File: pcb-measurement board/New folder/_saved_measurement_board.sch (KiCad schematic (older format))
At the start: 92 parts, among them P1 HDR DUAL ROW, P2 CONN_02X15, P3 CONN_02X13, P4 CONN_02X05, P5 CONN_02X05, Q1 Si1101X, U1 NX3L4051, U10 TLV1G125, U11 NX3L4051, U12 MSP430G2955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

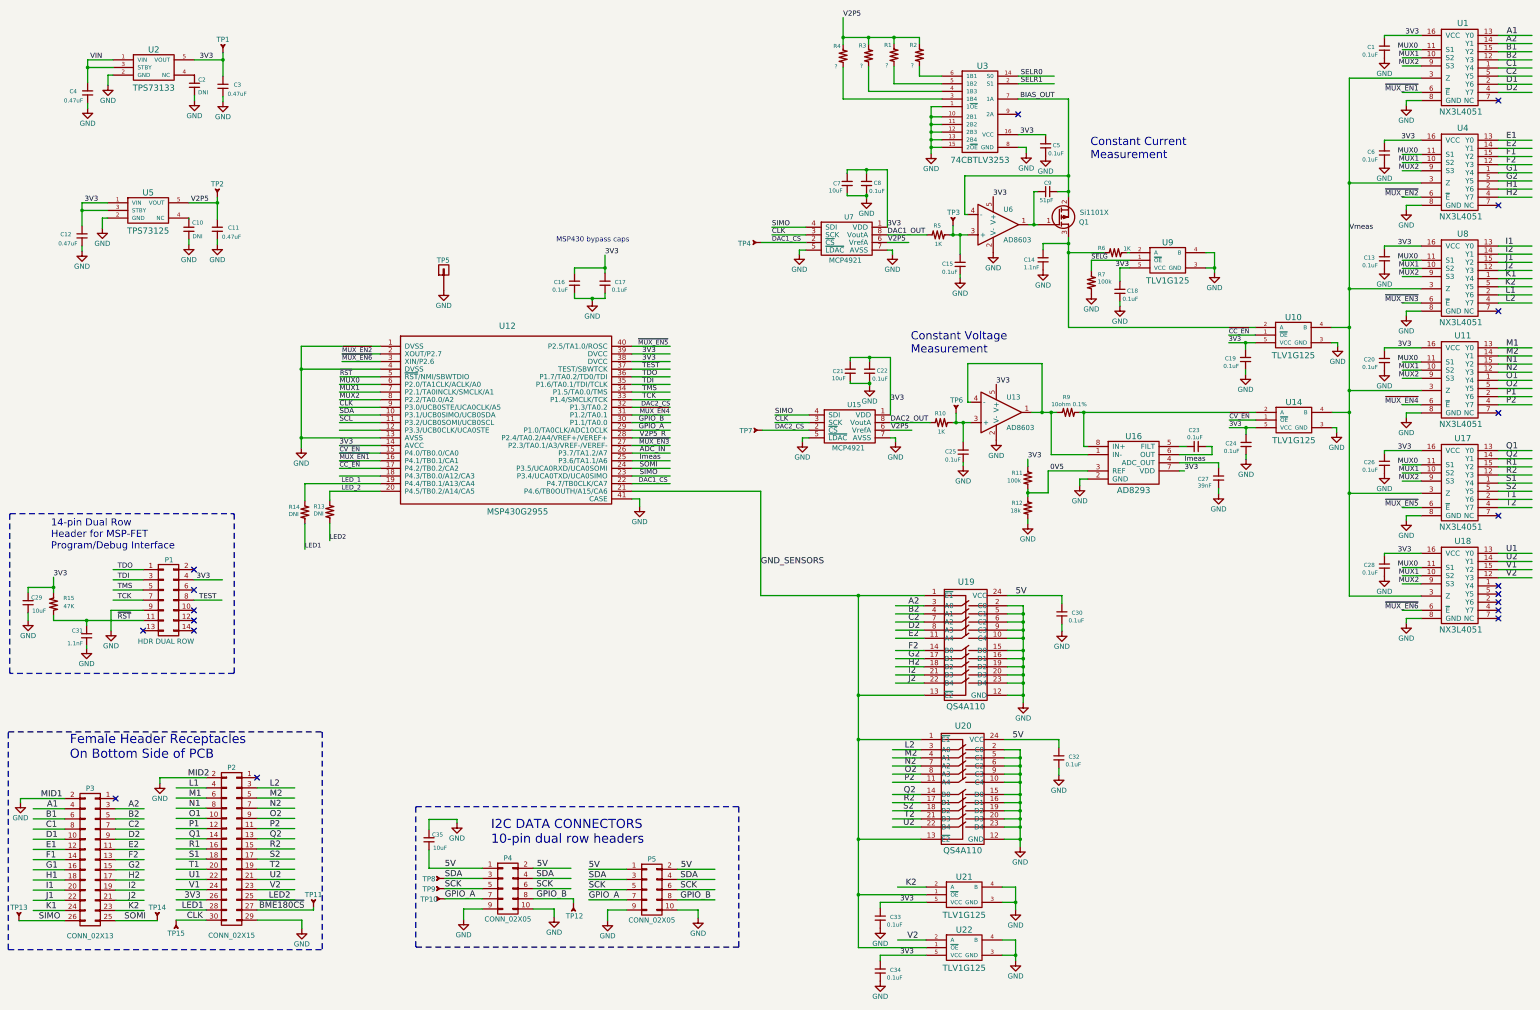
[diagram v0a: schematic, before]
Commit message: -replaced all measurement board 0402 components with 0603 -adjusted placement and started routing on the layout
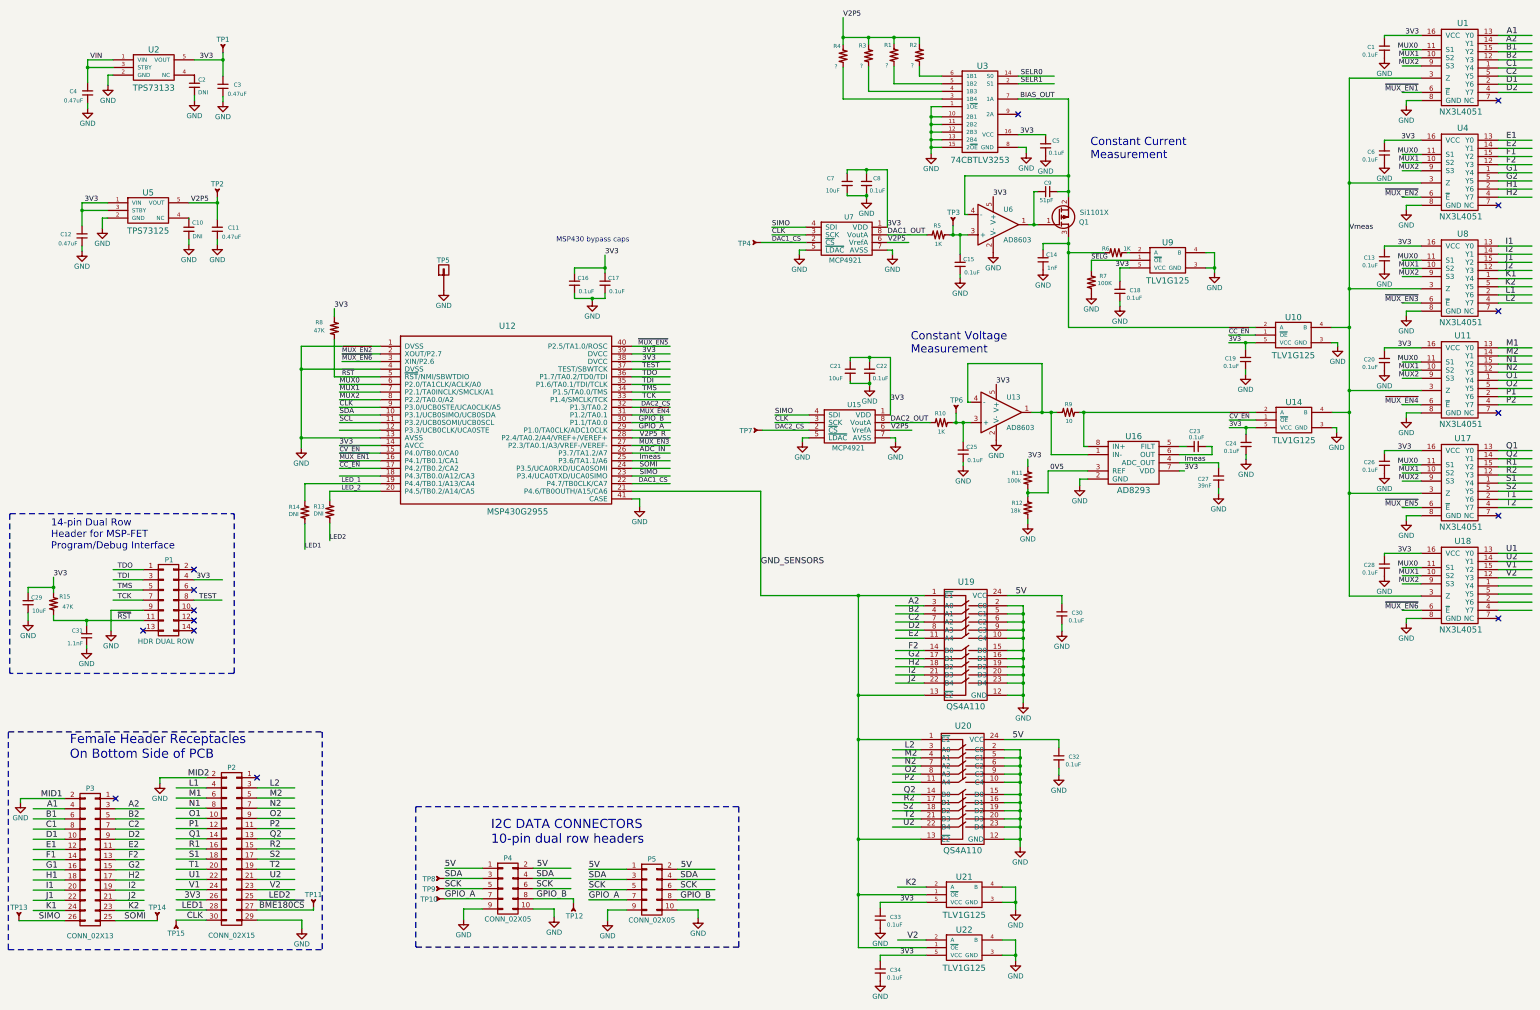
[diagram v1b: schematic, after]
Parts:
- removed C35: 10uF, footprints_on_Cdrive:0603, symbol CAP_NP
- removed R15: 47K, footprints_on_Cdrive:0603, symbol Res1_1
- added R15: 47K, footprints_on_Cdrive:0402, symbol Res1
- added R8: 47K, footprints_on_Cdrive:0402, symbol Res1_1
- C14: value 1.1nF -> 1nF; footprint footprints_on_Cdrive:0603 -> footprints_on_Cdrive:0402; description CAP CER 1100PF 50V C0G/NP0 0603 -> CAP CER 1000PF 50V X7R 0402; manufacturer pn GRM1885C1H112JA01D -> GRM155R71H102KA01D; supplier pn 490-1452-1-ND -> 490-1303-1-ND
- C15, C16, C17, C22, C23, C25, C5, C8: footprint footprints_on_Cdrive:0603 -> footprints_on_Cdrive:0402; description CAP CER 0.1UF 16V X7R 0603 -> CAP CER 0.1UF 16V X5R 0402; manufacturer pn GRM188R71C104KA01D -> 0402YD104KAT2A; supplier pn 490-1532-1-ND -> 478-1126-1-ND
- C18: footprint footprints_on_Cdrive:0603 -> Resistors_SMD:R_0603_HandSoldering
- C21, C7: footprint footprints_on_Cdrive:0603 -> footprints_on_Cdrive:0402; description CAP CER 10UF 6.3V X5R 0603 -> CAP CER 10UF 10V X5R 0402; manufacturer Murata -> Samsung; manufacturer pn GRM188R60J106ME47D -> CL05A106MP8NUB8; supplier pn 490-3896-1-ND -> 1276-6830-1-ND
- C27: footprint footprints_on_Cdrive:0603 -> footprints_on_Cdrive:0402; description CAP CER 0.039UF 16V X7R 0603 -> CAP CER 0.1UF 16V X5R 0402; manufacturer Kemet -> AVX Corporation; manufacturer pn C0603C393K4RACTU -> 0402YD104KAT2A; supplier pn 399-9078-1-ND -> 478-1126-1-ND
- C29: footprint footprints_on_Cdrive:0603 -> footprints_on_Cdrive:0402; description CAP CER 10UF 6.3V X5R 0603 -> CAP CER 10UF 4V X5R 0402; manufacturer pn GRM188R60J106ME47D -> GRM155R60G106ME44D; supplier pn 490-3896-1-ND -> 490-10693-1-ND
- C31: footprint footprints_on_Cdrive:0603 -> footprints_on_Cdrive:0402; description CAP CER 1100PF 50V C0G/NP0 0603 -> CAP CER 1100PF 50V NP0 0402; manufacturer Murata -> Kemet; manufacturer pn GRM1885C1H112JA01D -> C0402C112J5GAC7867; supplier pn 490-1452-1-ND -> 399-9948-1-ND
- C9: footprint footprints_on_Cdrive:0603 -> footprints_on_Cdrive:0402; description CAP CER 51PF 50V C0G/NP0 0603 -> CAP CER 51PF 50V NP0 0402; manufacturer pn GRM1885C1H510JA01D -> GRM1555C1H510JA01D; supplier pn 490-1420-1-ND -> 490-5944-1-ND
- R10, R5, R6: footprint footprints_on_Cdrive:0603 -> footprints_on_Cdrive:0402; description RES SMD 1K OHM 1% 1/10W 0603 -> RES SMD 1K OHM 1% 1/16W 0402; manufacturer pn RC0603FR-071KLL -> RC0402FR-071KL; supplier pn 311-1.00KHRCT-ND -> 311-1.00KLRCT-ND
- R11: footprint footprints_on_Cdrive:0603 -> footprints_on_Cdrive:0402; description RES SMD 100K OHM 1% 1/10W 0603 -> RES SMD 100K OHM 1% 1/16W 0402; manufacturer Yageo -> Stackpole Electronics Inc.; manufacturer pn RC0603FR-07100KL -> RC0402FR-07100KL; supplier pn 311-100KHRCT-ND -> 311-100KLRCT-ND
- R12: footprint footprints_on_Cdrive:0603 -> footprints_on_Cdrive:0402; description RES SMD 18K OHM 1% 1/10W 0603 -> RES SMD 100K OHM 1% 1/16W 0402; manufacturer Yageo -> Stackpole Electronics Inc.; manufacturer pn RC0603FR-0718KL -> RC0402FR-07100KL; supplier pn 311-18.0KHRCT-ND -> 311-100KLRCT-ND
- R7: value 100k -> 100K; footprint footprints_on_Cdrive:0603 -> footprints_on_Cdrive:0402; description RES SMD 100K OHM 1% 1/10W 0603 -> RES SMD 100K OHM 1% 1/16W 0402; manufacturer Yageo -> Stackpole Electronics Inc.; manufacturer pn RC0603FR-07100KL -> RC0402FR-07100KL; supplier pn 311-100KHRCT-ND -> 311-100KLRCT-ND
- R9: value 10ohm 0.1% -> 10; footprint footprints_on_Cdrive:0805 -> footprints_on_Cdrive:0402; description RES SMD 10 OHM 0.1% 1/4W 0805 -> RES SMD 100K OHM 1% 1/16W 0402; manufacturer TE Connectivity -> Stackpole Electronics Inc.; manufacturer pn 2-1625868-7 -> RC0402FR-07100KL; supplier pn A110351CT-ND -> 311-100KLRCT-ND
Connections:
- wire segments 476 -> 478
- no-connect marks 19 -> 15
